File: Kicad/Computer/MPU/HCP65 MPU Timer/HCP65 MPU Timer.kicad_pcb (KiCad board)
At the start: 2 copper layers, 18.8 x 43.3 mm, 20 parts, among them IC1 74LVC2G74DP,125, IC11 74LVC1G27GW,125, IC14 74HCT4040PW,118, IC2 74LVC273PW,118, IC5 AP7365-33WG-7, IC6 74HCT4040PW,118, IC7 PI3B3251QE, IC9 74LVC541APW,118, J1 Pin_Header_01x16, J2 Conn_02x16_Counter_Clockwise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

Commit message: Added GPIO Address Decoded for Pico and Pico Power.
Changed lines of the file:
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@@
     (fp_arc (start 8.509 -2.6162) (mid 7.62 -1.7272) (end 6.731 -2.6162)
       (stroke (width 0.1) (type default)) (layer "Edge.Cuts"))
-    (fp_arc (start 14.404267 -2.613733) (mid 16.252453 -1.848189) (end 17.017999 -0.000001)
+    (fp_arc (start 14.404267 -2.613733) (mid 16.25245 -1.848186) (end 17.017999 -0.000001)
       (stroke (width 0.1) (type solid)) (layer "Edge.Cuts"))
     (fp_arc (start 17.018 38.1) (mid 16.252456 39.948187) (end 14.404268 40.713732)

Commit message: Updated all MPU boards with new DIP footprint.
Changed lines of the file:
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@@
     (fp_arc (start 8.509 -2.6162) (mid 7.62 -1.7272) (end 6.731 -2.6162)
       (stroke (width 0.1) (type default)) (layer "Edge.Cuts"))
-    (fp_arc (start 14.404267 -2.613733) (mid 16.25245 -1.848186) (end 17.017999 -0.000001)
+    (fp_arc (start 14.404267 -2.613733) (mid 16.252448 -1.848183) (end 17.017999 -0.000001)
       (stroke (width 0.1) (type solid)) (layer "Edge.Cuts"))
     (fp_arc (start 17.018 38.1) (mid 16.252456 39.948187) (end 14.404268 40.713732)

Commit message: Generating MPU gerbers again with paste layers.
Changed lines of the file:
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@@
   )
   (paper "A4")
+  (title_block
+    (title "MPU Timer")
+    (date "2024-02-15")
+    (rev "V0")
+  )
   (layers
     (0 "F.Cu" signal)
     (31 "B.Cu" signal)
+    (34 "B.Paste" user)
+    (35 "F.Paste" user)
     (36 "B.SilkS" user "B.Silkscreen")
     (37 "F.SilkS" user "F.Silkscreen")
@@
     (grid_origin 88.9 58.42)
     (pcbplotparams
-      (layerselection 0x00010f0_ffffffff)
+      (layerselection 0x00010fc_ffffffff)
       (plot_on_all_layers_selection 0x0000000_00000000)
       (disableapertmacros false)
@@
       (viasonmask false)
       (mode 1)
-      (useauxorigin false)
+      (useauxorigin true)
       (hpglpennumber 1)
       (hpglpenspeed 20)
@@
     (fp_arc (start 8.509 -2.6162) (mid 7.62 -1.7272) (end 6.731 -2.6162)
       (stroke (width 0.1) (type default)) (layer "Edge.Cuts"))
-    (fp_arc (start 14.404267 -2.613733) (mid 16.252448 -1.848183) (end 17.017999 -0.000001)
+    (fp_arc (start 14.404267 -2.613733) (mid 16.252451 -1.848184) (end 17.017999 -0.000001)
       (stroke (width 0.1) (type solid)) (layer "Edge.Cuts"))
     (fp_arc (start 17.018 38.1) (mid 16.252456 39.948187) (end 14.404268 40.713732)

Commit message: Re-autorouted a bunch of boards.  Or something.  I don't know.
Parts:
- moved IC6 0.63 mm to (96.3, 80.9)
- moved C7 0.42 mm to (100.1, 66.0)
- moved C10 0.25 mm to (100.6, 86.1)
- moved C11 0.13 mm to (99.6, 79.5)
- moved C6 0.13 mm to (93.5, 92.2)
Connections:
- J2 pad 10: /D5 -> /D2
- J2 pad 11: /D4 -> /D3
- J2 pad 13: /D3 -> /D4
- J2 pad 14: /D2 -> /D5
- J2 pad 15: /D1 -> /D6
- J2 pad 16: /D0 -> /D7
- J2 pad 8: /D7 -> /D0
- J2 pad 9: /D6 -> /D1
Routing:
- net /D3: track 3.76 -> 10.4 mm
- net /D5: track 9.80 -> 4.21 mm, vias 0 -> 1
- net /D2: track 37.0 -> 42.1 mm, vias 2 -> 3
- net /D1: track 43.2 -> 47.5 mm, vias 2 -> 3
- net /D6: track 11.5 -> 8.11 mm, vias 0 -> 1
- net /Q16: track 12.4 -> 14.7 mm
- net /Q8: track 18.5 -> 16.6 mm
- net /D7: track 12.6 -> 11.0 mm
- net /GND: track 230.2 -> 231.7 mm
- net /Q20: track 12.9 -> 11.6 mm
- net /Q6: track 17.2 -> 18.4 mm
- net /Q0: track 20.0 -> 18.9 mm
- net /Q10: track 16.6 -> 17.6 mm
- net /~{RD}: track 34.7 -> 35.7 mm
- net /3.3V: track 85.5 -> 84.6 mm
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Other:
- board text added: "MPU TIME V1"
- board text removed: "MPU TIME V0"

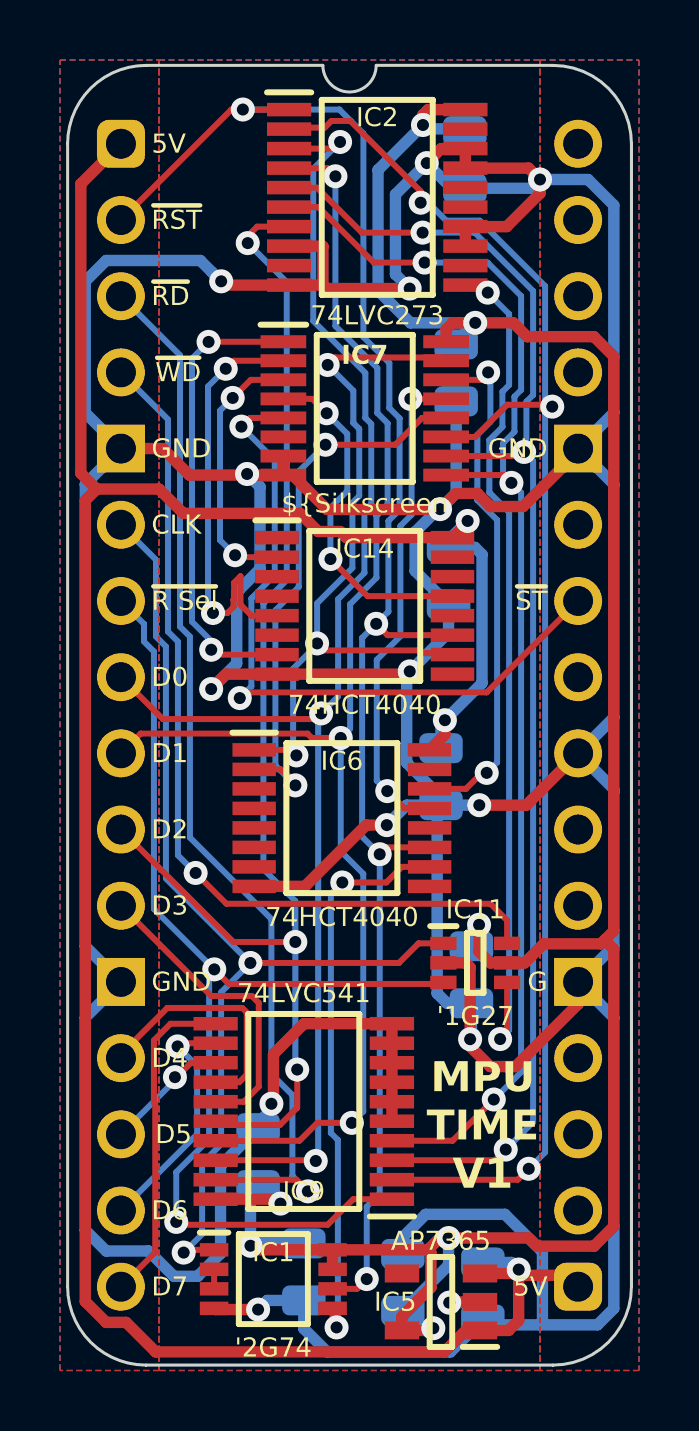
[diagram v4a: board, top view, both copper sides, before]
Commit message: Manually re-routing the Small Mainboard.
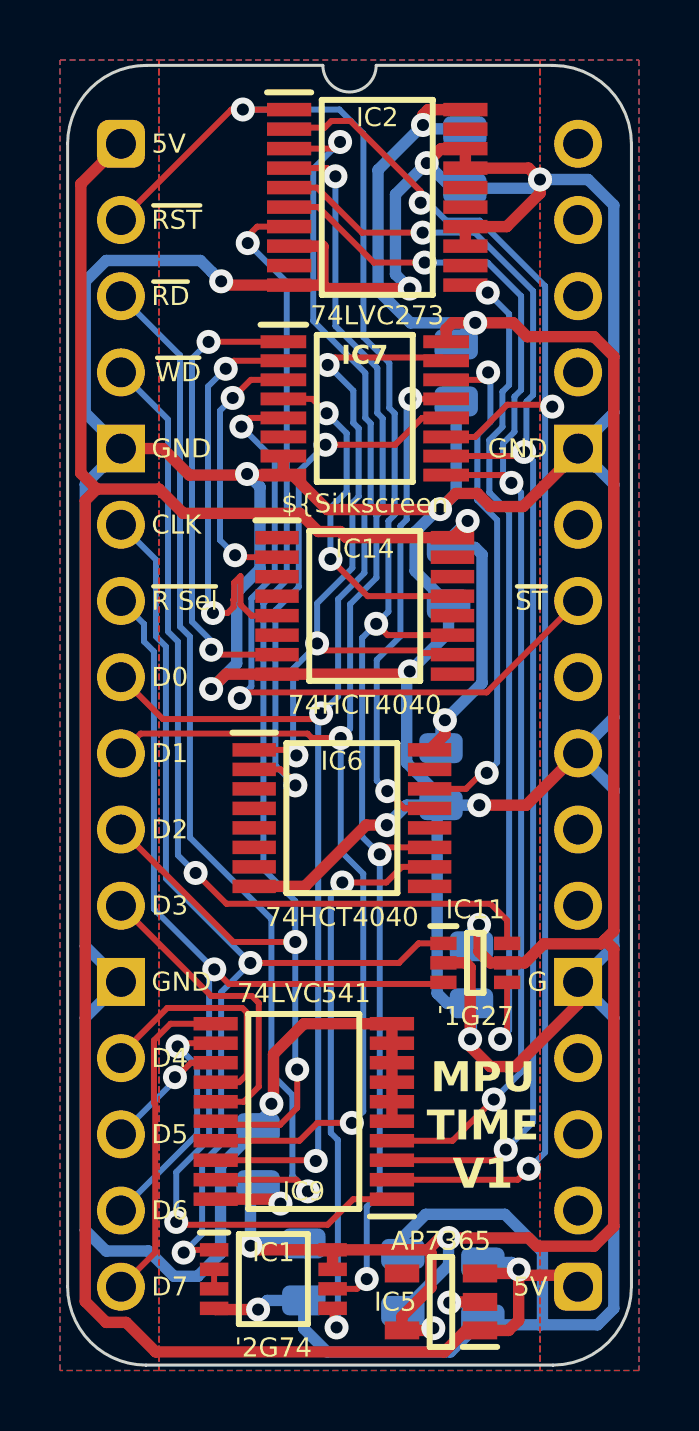
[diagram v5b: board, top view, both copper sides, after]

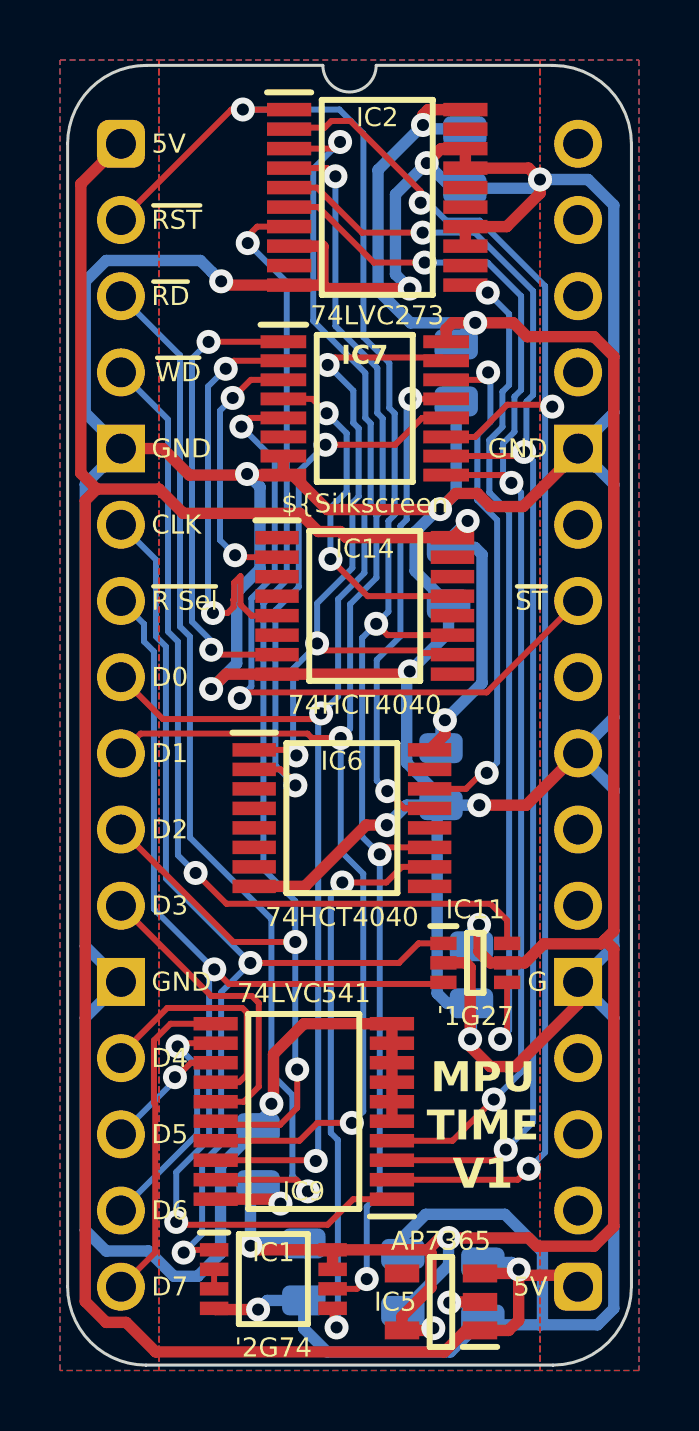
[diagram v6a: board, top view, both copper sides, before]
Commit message: Converted more PCBs to Kicad 8.
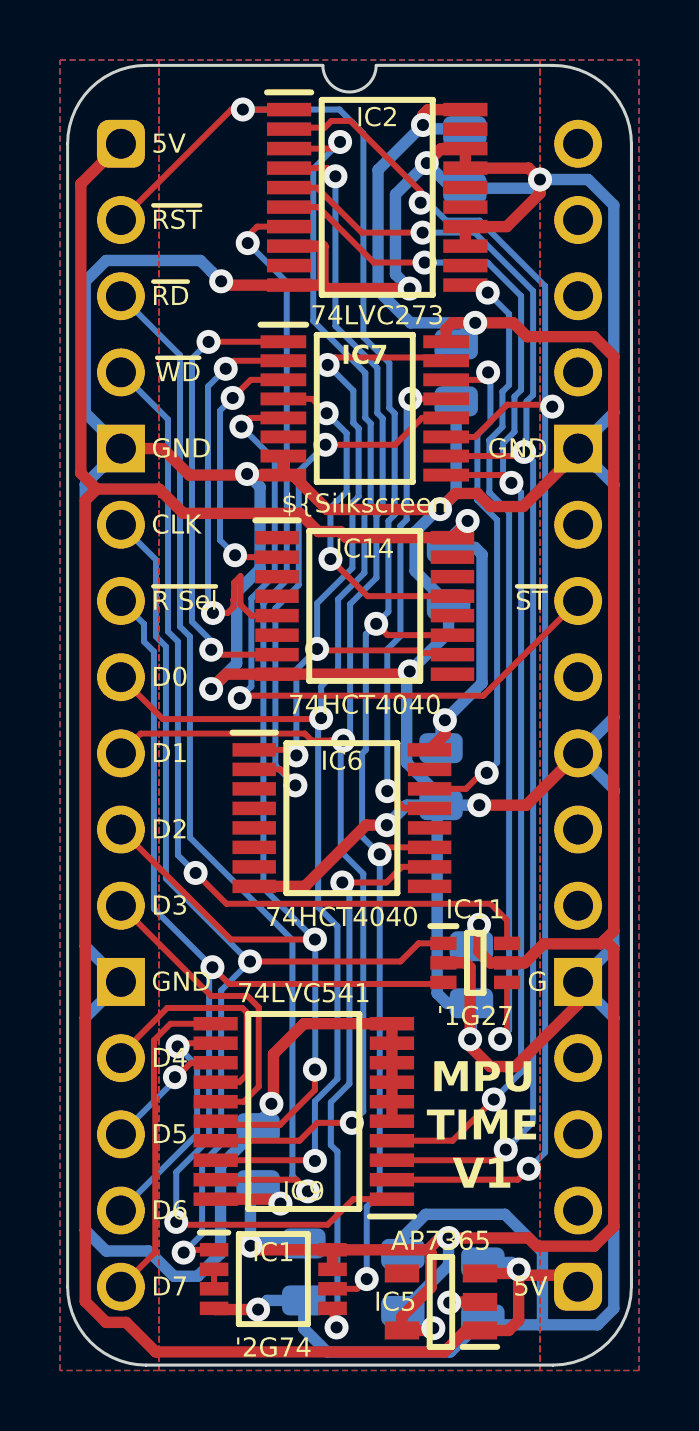
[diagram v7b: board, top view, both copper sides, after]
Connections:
- net /5V renamed 5V
- net /CLK renamed CLK
- net /D0 renamed D0
- net /D1 renamed D1
- net /D2 renamed D2
- net /D3 renamed D3
- net /D4 renamed D4
- net /D5 renamed D5
- net /D6 renamed D6
- net /D7 renamed D7
- net /GND renamed GND
- net /~{NMI Rate Select} renamed ~{NMI Rate Select}
- net /~{RD} renamed ~{RD}
- net /~{Reset} renamed ~{Reset}
- net /~{Set Timer} renamed ~{Set Timer}
- net /~{WD} renamed ~{WD}
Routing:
- net D2: track 42.1 -> 43.2 mm

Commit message: Added a (potentially) 50MHz board.
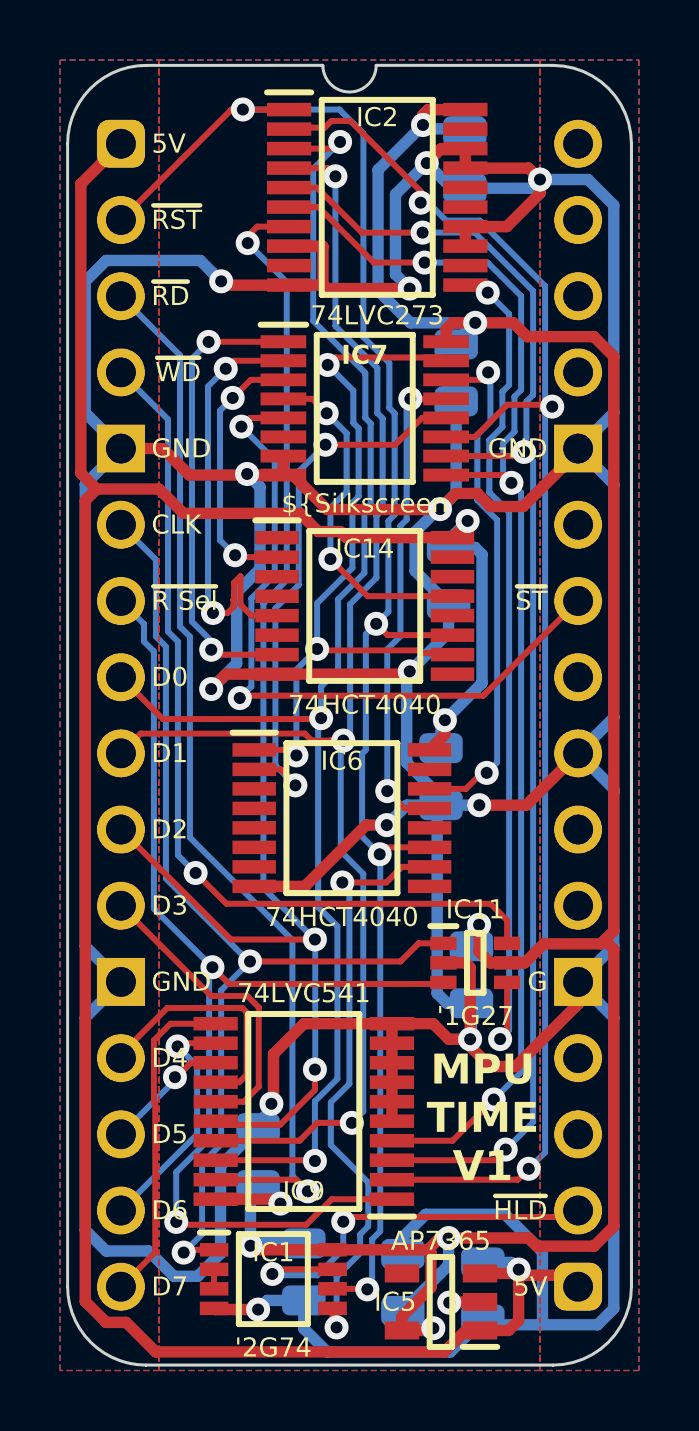
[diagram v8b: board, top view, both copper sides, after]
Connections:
- IC1 pad 7: /3.3V -> ~{Hold}
- J2 pad 18: unconnected-(J2-Pin_18-Pad18) -> ~{Hold}
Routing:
- net ~{Hold}: track 0.00 -> 13.4 mm, vias 0 -> 2
- net GND: track 231.7 -> 234.5 mm
- net /Q0: track 19.1 -> 20.0 mm
- net /3.3V: track 84.6 -> 84.0 mm
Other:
- board text added: "~{HLD}"
